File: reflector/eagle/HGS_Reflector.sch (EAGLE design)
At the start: 28 parts, among them J1 U.FL, U3 LP2985XX-N

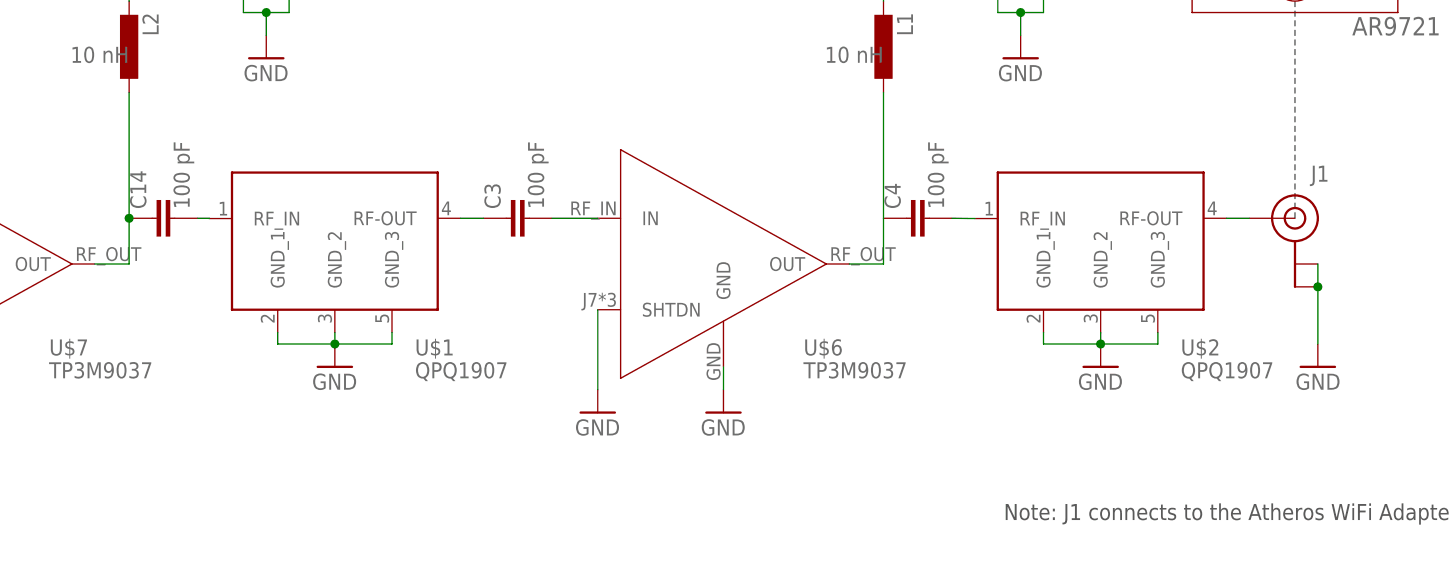
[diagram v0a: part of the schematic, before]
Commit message: I checked that all parts in the HGS schematic/board are up to date with the current footprints.
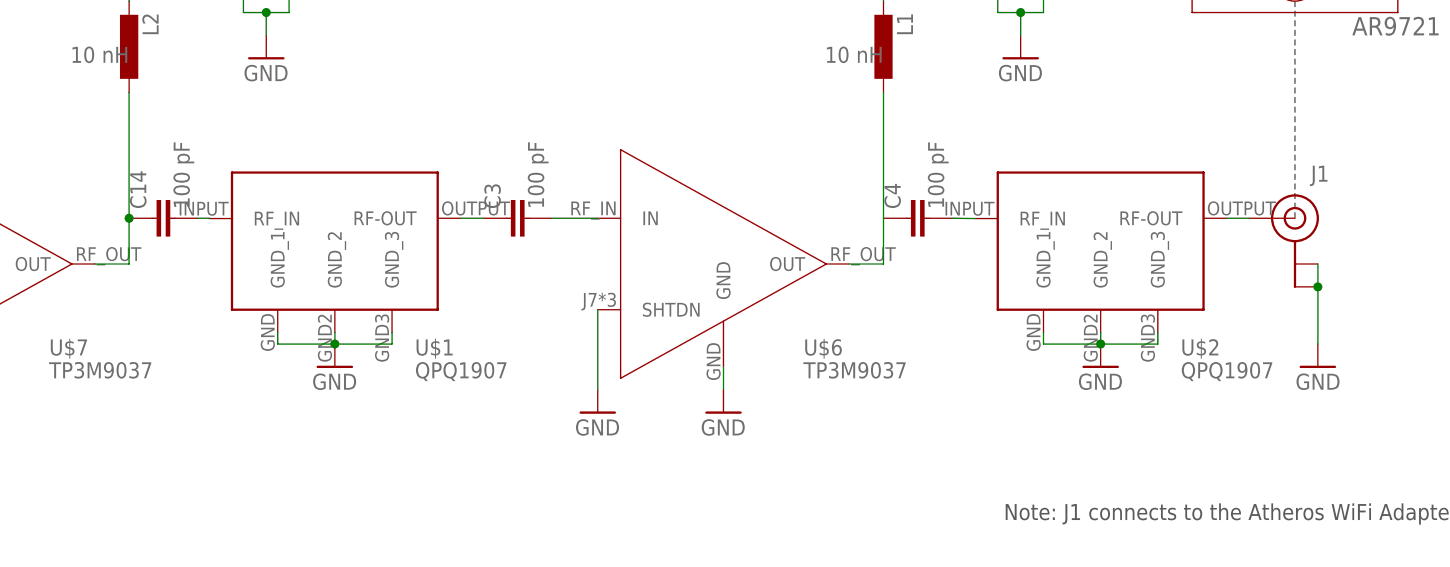
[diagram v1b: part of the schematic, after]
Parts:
- U$1, U$2: value BPFQPQ1907 -> BPF; device HGS_Data_Parts:BPFQPQ1907 -> QPQ1907_BPF:BPF
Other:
- moved on the sheet: U$1, U$2
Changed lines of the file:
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@@
 <part name="GND13" library="supply1" library_urn="urn:adsk.eagle:library:371" deviceset="GND" device=""/>
 <part name="C9" library="ngspice-simulation" library_urn="urn:adsk.eagle:library:527439" deviceset="C" device="" value="2.2 uF"/>
-<part name="U$1" library="HGS_Data_Parts" deviceset="BPF" device="QPQ1907"/>
 <part name="GND15" library="supply1" library_urn="urn:adsk.eagle:library:371" deviceset="GND" device="">
 <attribute name="SPICEPREFIX" value="G"/>
@@
 <part name="U$6" library="HGS_Data_Parts" deviceset="LNA-TP3M9037" device=""/>
 <part name="GND4" library="supply1" library_urn="urn:adsk.eagle:library:371" deviceset="GND" device=""/>
-<part name="U$2" library="HGS_Data_Parts" deviceset="BPF" device="QPQ1907"/>
 <part name="GND7" library="supply1" library_urn="urn:adsk.eagle:library:371" deviceset="GND" device=""/>
 <part name="C1" library="oresat-rcl" deviceset="C-EU" device="0603-C-NOSILK" value="100 pF"/>
@@
 <attribute name="_EXTERNAL_" value="1 uF"/>
 </part>
+<part name="U$1" library="QPQ1907_BPF" deviceset="BPF" device=""/>
+<part name="U$2" library="QPQ1907_BPF" deviceset="BPF" device=""/>
 </parts>
 <sheets>
@@
 <attribute name="VALUE" x="85.09" y="191.77" size="1.778" layer="96" rot="R90"/>
 </instance>
-<instance part="U$1" gate="G$1" x="139.7" y="110.49" smashed="yes">
-<attribute name="NAME" x="148.59" y="97.79" size="1.778" layer="95"/>
-</instance>
 <instance part="GND15" gate="1" x="85.09" y="91.44" smashed="yes">
 <attribute name="VALUE" x="82.55" y="88.9" size="1.778" layer="96"/>
@@
 <instance part="GND4" gate="1" x="224.79" y="96.52" smashed="yes">
 <attribute name="VALUE" x="222.25" y="93.98" size="1.778" layer="96"/>
-</instance>
-<instance part="U$2" gate="G$1" x="224.79" y="110.49" smashed="yes">
-<attribute name="NAME" x="233.68" y="97.79" size="1.778" layer="95"/>
 </instance>
 <instance part="GND7" gate="1" x="215.9" y="130.81" smashed="yes">
@@
 <attribute name="NAME" x="38.1" y="179.07" size="1.778" layer="95"/>
 <attribute name="VALUE" x="34.29" y="176.53" size="1.778" layer="96"/>
+</instance>
+<instance part="U$1" gate="G$1" x="139.7" y="110.49" smashed="yes">
+<attribute name="NAME" x="148.59" y="97.79" size="1.778" layer="95"/>
+</instance>
+<instance part="U$2" gate="G$1" x="224.79" y="110.49" smashed="yes">
+<attribute name="NAME" x="233.68" y="97.79" size="1.778" layer="95"/>
 </instance>
 </instances>
@@
 <segment>
 <pinref part="C3" gate="CE" pin="1"/>
+<wire x1="156.21" y1="113.03" x2="153.67" y2="113.03" width="0.1524" layer="91"/>
 <pinref part="U$1" gate="G$1" pin="RF-OUT"/>
-<wire x1="156.21" y1="113.03" x2="153.67" y2="113.03" width="0.1524" layer="91"/>
 </segment>
 </net>
@@
 <segment>
 <pinref part="J1" gate="G$1" pin="SIGNAL"/>
+<wire x1="241.3" y1="113.03" x2="238.76" y2="113.03" width="0.1524" layer="91"/>
 <pinref part="U$2" gate="G$1" pin="RF-OUT"/>
-<wire x1="241.3" y1="113.03" x2="238.76" y2="113.03" width="0.1524" layer="91"/>
 </segment>
 </net>
@@
 <segment>
 <pinref part="C4" gate="CE" pin="2"/>
+<wire x1="208.28" y1="113.03" x2="210.82" y2="113" width="0.1524" layer="91"/>
 <pinref part="U$2" gate="G$1" pin="RF_IN"/>
-<wire x1="208.28" y1="113.03" x2="210.82" y2="113" width="0.1524" layer="91"/>
 </segment>
 </net>
@@
 <segment>
 <pinref part="C14" gate="CE" pin="2"/>
-<pinref part="U$1" gate="G$1" pin="RF_IN"/>
 <wire x1="124.46" y1="113.03" x2="125.73" y2="113.03" width="0.1524" layer="91"/>
 <wire x1="125.73" y1="113.03" x2="125.73" y2="113" width="0.1524" layer="91"/>
-</segment>
-</net>
+<pinref part="U$1" gate="G$1" pin="RF_IN"/>
+</segment>
+</net>

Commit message: I made updates to the HGS board.
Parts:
- removed PI_USB_OUT1: (no value), con-amp:USB-787616
- U$4: device HGS_Data_Parts:AR9721 -> AR9721:AR9721
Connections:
- net 1: no longer PI_USB_OUT1.1
- net N$18: no longer PI_USB_OUT1.2
- net N$19: no longer PI_USB_OUT1.3
- net VCC: no longer PI_USB_OUT1.4
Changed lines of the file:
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@@
 <?xml version="1.0" encoding="utf-8"?>
 <!DOCTYPE eagle SYSTEM "eagle.dtd">
-<eagle version="9.4.2">
+<eagle version="9.6.2">
 <drawing>
 <settings>
@@
 <part name="3.3V1" library="oresat-supplies" deviceset="3.3V" device=""/>
 <part name="U$3" library="HGS_Data_Parts" deviceset="1/4_WAVE_TRF" device=""/>
-<part name="PI_USB_OUT1" library="con-amp" library_urn="urn:adsk.eagle:library:127" deviceset="USB-787616" device="" package3d_urn="urn:adsk.eagle:package:8081650/1"/>
 <part name="3.3V4" library="oresat-supplies" deviceset="3.3V" device=""/>
 <part name="C14" library="oresat-rcl" deviceset="C-EU" device="0402-C-NOSILK" value="100 pF"/>
@@
 <part name="3.3V3" library="oresat-supplies" deviceset="3.3V" device=""/>
 <part name="C4" library="oresat-rcl" deviceset="C-EU" device="0402-C-NOSILK" value="100 pF"/>
-<part name="U$4" library="HGS_Data_Parts" deviceset="AR9721" device=""/>
 <part name="L2" library="rcl" library_urn="urn:adsk.eagle:library:334" deviceset="L-EU" device="L3216C" package3d_urn="urn:adsk.eagle:package:23476/2">
 <spice>
@@
 <part name="U$1" library="QPQ1907_BPF" deviceset="BPF" device=""/>
 <part name="U$2" library="QPQ1907_BPF" deviceset="BPF" device=""/>
+<part name="U$4" library="AR9721" deviceset="AR9721" device=""/>
 </parts>
 <sheets>
@@
 <attribute name="NAME" x="55.88" y="102.87" size="1.778" layer="95"/>
 </instance>
-<instance part="PI_USB_OUT1" gate="G$1" x="246.38" y="179.07" smashed="yes" rot="R90">
-<attribute name="VALUE" x="254" y="175.26" size="1.778" layer="96" rot="R90"/>
-</instance>
 <instance part="3.3V4" gate="G$1" x="76.2" y="196.85" smashed="yes">
 <attribute name="VALUE" x="73.66" y="196.85" size="1.778" layer="96"/>
@@
 <attribute name="VALUE" x="207.391" y="114.046" size="1.778" layer="96" rot="R90"/>
 </instance>
-<instance part="U$4" gate="G$1" x="246.38" y="143.51" smashed="yes"/>
 <instance part="L2" gate="G$1" x="116.84" y="132.08" smashed="yes" rot="R180">
 <attribute name="NAME" x="118.3386" y="135.89" size="1.778" layer="95" rot="R270"/>
@@
 <attribute name="NAME" x="233.68" y="97.79" size="1.778" layer="95"/>
 </instance>
+<instance part="U$4" gate="G$1" x="246.38" y="143.51" smashed="yes"/>
 </instances>
 <busses>
@@
 <pinref part="PI_USB_OUT" gate="G$1" pin="1"/>
 <label x="241.3" y="171.45" size="1.778" layer="95" rot="R90"/>
-<pinref part="PI_USB_OUT1" gate="G$1" pin="1"/>
 <label x="241.3" y="171.45" size="1.778" layer="95" rot="R90"/>
 <wire x1="238.76" y1="153.67" x2="238.76" y2="173.99" width="0.1524" layer="91"/>
@@
 <net name="N$18" class="0">
 <segment>
-<pinref part="PI_USB_OUT1" gate="G$1" pin="2"/>
 <pinref part="PI_USB_OUT" gate="G$1" pin="2"/>
 <wire x1="243.84" y1="173.99" x2="243.84" y2="171.45" width="0.1524" layer="91"/>
@@
 <net name="N$19" class="0">
 <segment>
-<pinref part="PI_USB_OUT1" gate="G$1" pin="3"/>
 <wire x1="243.84" y1="153.67" x2="243.84" y2="170.18" width="0.1524" layer="91"/>
 <wire x1="243.84" y1="170.18" x2="246.38" y2="170.18" width="0.1524" layer="91"/>
@@
 </segment>
 </net>
+<net name="N$3" class="0">
+<segment>
+<pinref part="C4" gate="CE" pin="2"/>
+<wire x1="208.28" y1="113.03" x2="210.82" y2="113" width="0.1524" layer="91"/>
+<pinref part="U$2" gate="G$1" pin="RF_IN"/>
+</segment>
+</net>
+<net name="N$6" class="0">
+<segment>
+<pinref part="C14" gate="CE" pin="2"/>
+<wire x1="124.46" y1="113.03" x2="125.73" y2="113.03" width="0.1524" layer="91"/>
+<wire x1="125.73" y1="113.03" x2="125.73" y2="113" width="0.1524" layer="91"/>
+<pinref part="U$1" gate="G$1" pin="RF_IN"/>
+</segment>
+</net>
+<net name="N$7" class="0">
+<segment>
+<pinref part="L3" gate="G$1" pin="1"/>
+<pinref part="L2" gate="G$1" pin="2"/>
+<wire x1="116.84" y1="138.43" x2="116.84" y2="137.16" width="0.1524" layer="91"/>
+</segment>
+</net>
+<net name="3.3V1" class="0">
+<segment>
+<pinref part="L4" gate="G$1" pin="2"/>
+<wire x1="200.66" y1="148.59" x2="200.66" y2="151.13" width="0.1524" layer="91"/>
+</segment>
+</net>
+<net name="N$13" class="0">
+<segment>
+<wire x1="200.66" y1="113.03" x2="200.66" y2="127" width="0.1524" layer="91"/>
+<pinref part="L1" gate="G$1" pin="1"/>
+</segment>
+</net>
+<net name="N$14" class="0">
+<segment>
+<pinref part="L4" gate="G$1" pin="1"/>
+<pinref part="L1" gate="G$1" pin="2"/>
+<wire x1="200.66" y1="138.43" x2="200.66" y2="137.16" width="0.1524" layer="91"/>
+</segment>
+</net>
 <net name="VCC" class="0">
 <segment>
-<pinref part="PI_USB_OUT1" gate="G$1" pin="4"/>
 <pinref part="PI_USB_OUT" gate="G$1" pin="4"/>
 <wire x1="248.92" y1="173.99" x2="254" y2="173.99" width="0.1524" layer="91"/>
@@
 </segment>
 </net>
-<net name="N$3" class="0">
-<segment>
-<pinref part="C4" gate="CE" pin="2"/>
-<wire x1="208.28" y1="113.03" x2="210.82" y2="113" width="0.1524" layer="91"/>
-<pinref part="U$2" gate="G$1" pin="RF_IN"/>
-</segment>
-</net>
-<net name="N$6" class="0">
-<segment>
-<pinref part="C14" gate="CE" pin="2"/>
-<wire x1="124.46" y1="113.03" x2="125.73" y2="113.03" width="0.1524" layer="91"/>
-<wire x1="125.73" y1="113.03" x2="125.73" y2="113" width="0.1524" layer="91"/>
-<pinref part="U$1" gate="G$1" pin="RF_IN"/>
-</segment>
-</net>
-<net name="N$7" class="0">
-<segment>
-<pinref part="L3" gate="G$1" pin="1"/>
-<pinref part="L2" gate="G$1" pin="2"/>
-<wire x1="116.84" y1="138.43" x2="116.84" y2="137.16" width="0.1524" layer="91"/>
-</segment>
-</net>
-<net name="3.3V1" class="0">
-<segment>
-<pinref part="L4" gate="G$1" pin="2"/>
-<wire x1="200.66" y1="148.59" x2="200.66" y2="151.13" width="0.1524" layer="91"/>
-</segment>
-</net>
-<net name="N$13" class="0">
-<segment>
-<wire x1="200.66" y1="113.03" x2="200.66" y2="127" width="0.1524" layer="91"/>
-<pinref part="L1" gate="G$1" pin="1"/>
-</segment>
-</net>
-<net name="N$14" class="0">
-<segment>
-<pinref part="L4" gate="G$1" pin="1"/>
-<pinref part="L1" gate="G$1" pin="2"/>
-<wire x1="200.66" y1="138.43" x2="200.66" y2="137.16" width="0.1524" layer="91"/>
-</segment>
-</net>
